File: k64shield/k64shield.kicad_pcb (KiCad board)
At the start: 2 copper layers, 65 x 70.4 mm, 9 parts, among them J1 top_left_header_02x08, J2 bottom_left_header_02x06, J3 rpi_motor_driver_header, J4 top_right_header_02x10, J5 bottom_right_header_02x08, J6 camera_header_01x05, J7 servo_header_01x03

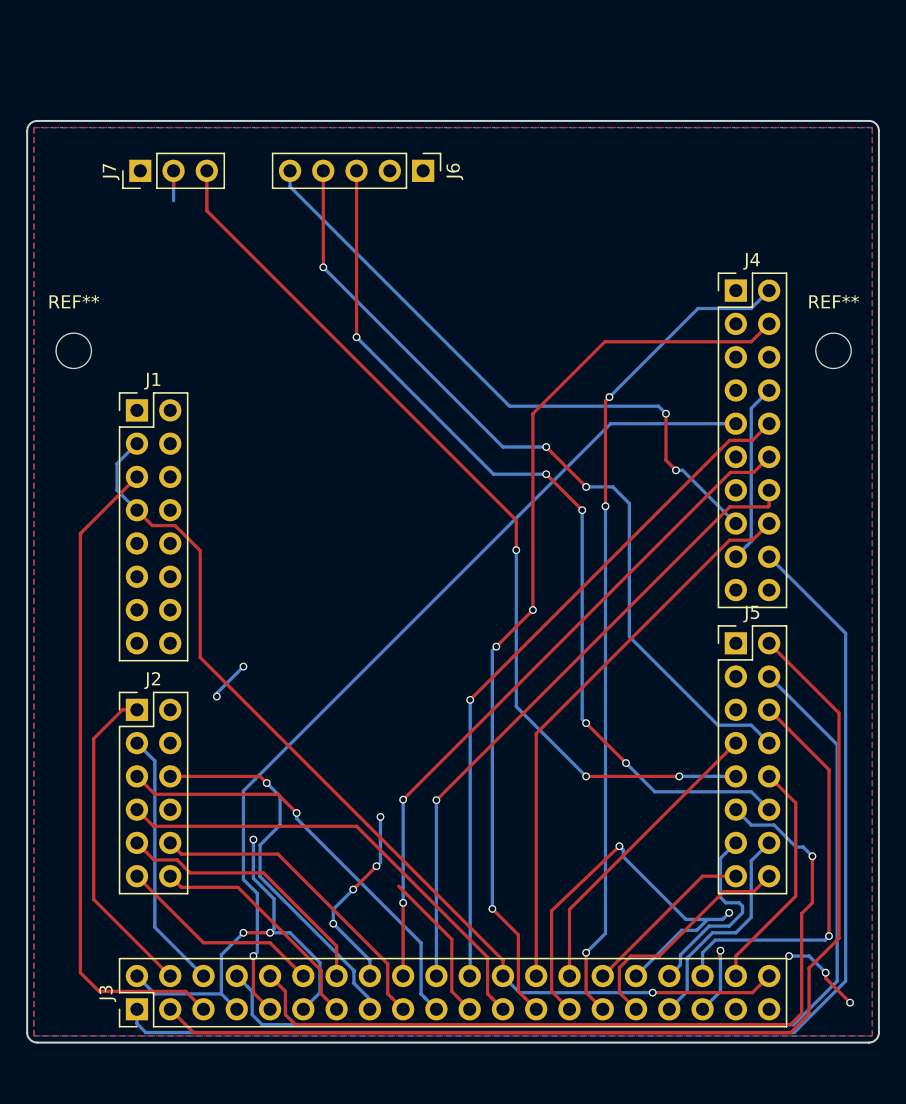
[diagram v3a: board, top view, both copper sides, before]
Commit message: added title and names to silk screen
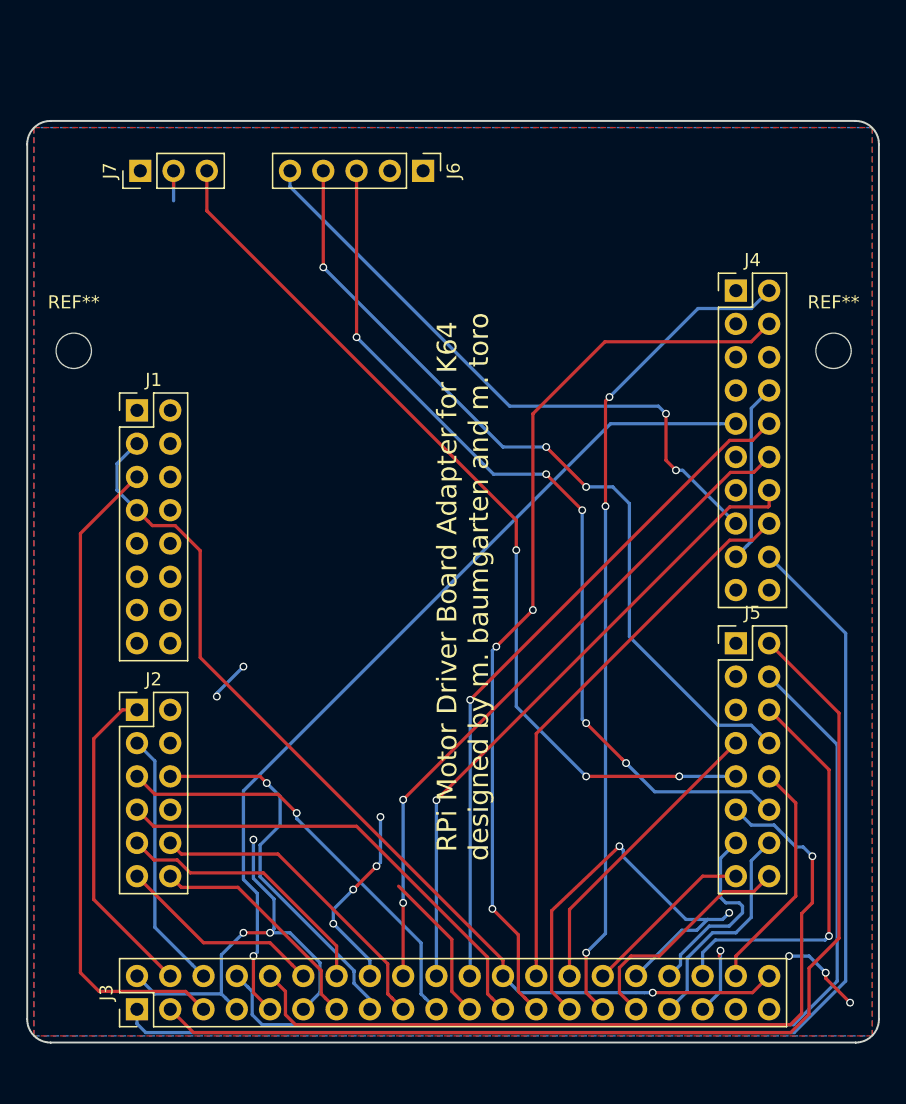
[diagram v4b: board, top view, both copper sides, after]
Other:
- outline, holes or cut-outs redrawn
- board text added: "RPi Motor Driver Board Adapter for K64 designed by m. baumgarten and m. toro"
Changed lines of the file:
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@@
   (general
     (thickness 1.6)
-    (drawings 8)
+    (drawings 9)
     (tracks 379)
     (zones 0)
@@
     (visible_elements 7FFFFFFF)
     (pcbplotparams
-      (layerselection 0x00030_80000001)
+      (layerselection 0x010f0_ffffffff)
       (usegerberextensions false)
       (usegerberattributes false)
@@
       (outputformat 1)
       (mirror false)
-      (drillshape 1)
+      (drillshape 0)
       (scaleselection 1)
-      (outputdirectory ""))
+      (outputdirectory "gerber/"))
   )
   (net 0 "")
@@
     (pad 1 np_thru_hole circle (at 0 0) (size 2.7 2.7) (drill 2.7) (layers *.Cu *.Mask))
   )
-  (gr_line (start 88.392 54.864) (end 88.392 123.698) (angle 90) (layer Edge.Cuts) (width 0.15))
-  (gr_line (start 152.654 54.102) (end 89.154 54.102) (angle 90) (layer Edge.Cuts) (width 0.15))
-  (gr_line (start 153.416 123.698) (end 153.416 54.864) (angle 90) (layer Edge.Cuts) (width 0.15))
-  (gr_line (start 89.154 124.46) (end 152.654 124.46) (angle 90) (layer Edge.Cuts) (width 0.15))
-  (gr_arc (start 89.154 54.864) (end 88.392 54.864) (angle 90) (layer Edge.Cuts) (width 0.15))
-  (gr_arc (start 152.654 54.864) (end 152.654 54.102) (angle 90) (layer Edge.Cuts) (width 0.15))
-  (gr_arc (start 152.654 123.698) (end 153.416 123.698) (angle 90) (layer Edge.Cuts) (width 0.15))
-  (gr_arc (start 89.154 123.698) (end 89.154 124.46) (angle 90) (layer Edge.Cuts) (width 0.15))
+  (gr_text "RPi Motor Driver Board Adapter for K64\ndesigned by m. baumgarten and m. toro" (at 121.666 89.662 90) (layer F.SilkS)
+    (effects (font (size 1.5 1.5) (thickness 0.3)))
+  )
+  (gr_line (start 90.17 124.46) (end 151.638 124.46) (layer Edge.Cuts) (width 0.15))
+  (gr_line (start 88.392 55.88) (end 88.392 122.682) (layer Edge.Cuts) (width 0.15))
+  (gr_line (start 151.638 54.102) (end 90.17 54.102) (layer Edge.Cuts) (width 0.15))
+  (gr_line (start 153.416 122.682) (end 153.416 55.88) (layer Edge.Cuts) (width 0.15))
+  (gr_arc (start 90.17 55.88) (end 90.17 54.102) (angle -90) (layer Edge.Cuts) (width 0.15))
+  (gr_arc (start 151.638 55.88) (end 153.416 55.88) (angle -90) (layer Edge.Cuts) (width 0.15))
+  (gr_arc (start 151.638 122.682) (end 151.638 124.46) (angle -90) (layer Edge.Cuts) (width 0.15))
+  (gr_arc (start 90.17 122.682) (end 88.392 122.682) (angle -90) (layer Edge.Cuts) (width 0.15))
   (segment (start 102.87 98.044) (end 102.87 98.044) (width 0.25) (layer B.Cu) (net 8))
   (segment (start 102.87 97.79) (end 104.902 95.758) (width 0.25) (layer B.Cu) (net 8))

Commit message: moved pins so enable were connected to gpio
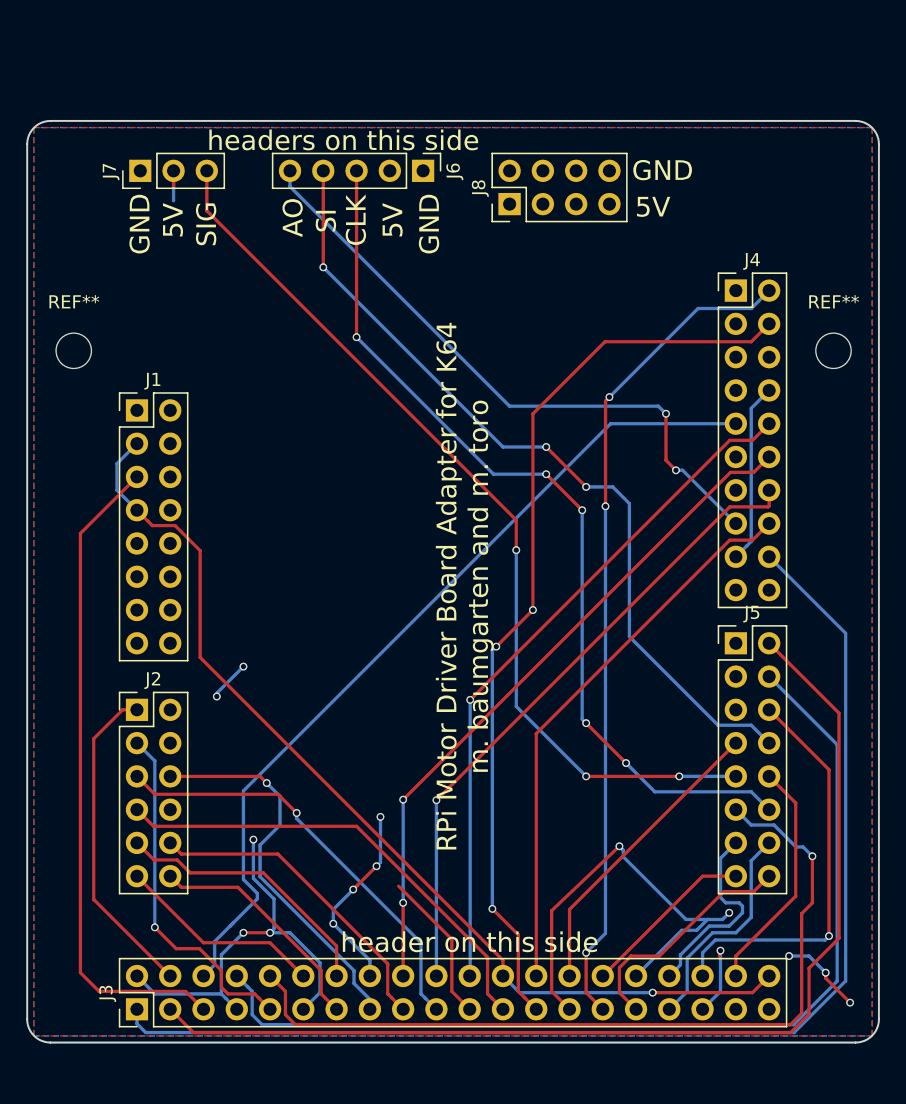
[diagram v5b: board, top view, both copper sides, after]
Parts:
- added J8: Conn_02x04_Top_Bottom, Pin_Headers:Pin_Header_Straight_2x04_Pitch2.54mm, F.Cu at (125.2, 60.5)
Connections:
- J3 pad 6: /PTB3 -> /ADC1_DP0
- J3 pad 9: /ADC1_DP0 -> /PTB3
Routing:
- net /PTB3: track 19.9 -> 26.8 mm, vias 0 -> 1
- net /ADC1_DP0: track 67.0 -> 65.8 mm, vias 1 -> 0
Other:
- board text added: "5V"
- board text added: "AO"
- board text added: "CLK"
- board text added: "GND"
- board text added: "RPi Motor Driver Board Adapter for K64 m. baumgarten and m. toro"
- board text added: "SI"
- board text added: "SIG"
- board text added: "header on this side"
- board text added: "headers on this side"
- board text removed: "RPi Motor Driver Board Adapter for K64 designed by m. baumgarten and m. toro"
